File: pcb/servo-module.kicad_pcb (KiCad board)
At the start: 4 copper layers, 50 x 30 mm, 77 parts, among them J10 Power Out, J2 QWICC, J5 QWICC, J7 Power In, J9 AVR-UPDI-6, U1 ATtiny1616-MNR

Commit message: Updated worksheet template and logo
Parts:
- removed LOGO2: ~, CRGM Logos:FNWW Face 8mm
- added LOGO4: ~, CRGM Logos:CRGM Logo 5mm, B.Cu at (56.1, 153.1)
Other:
- board text removed: "FNWW"

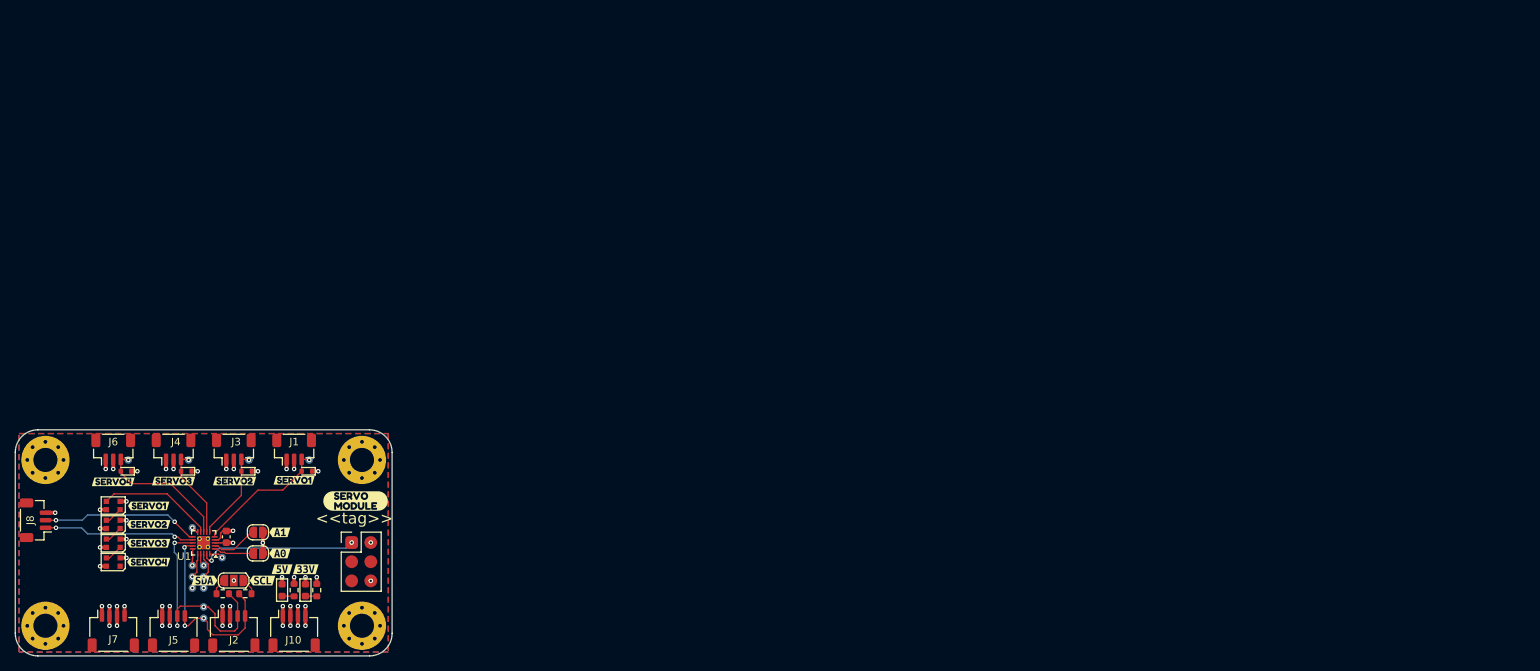
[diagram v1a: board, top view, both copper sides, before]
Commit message: Standardized parts; fixed title box
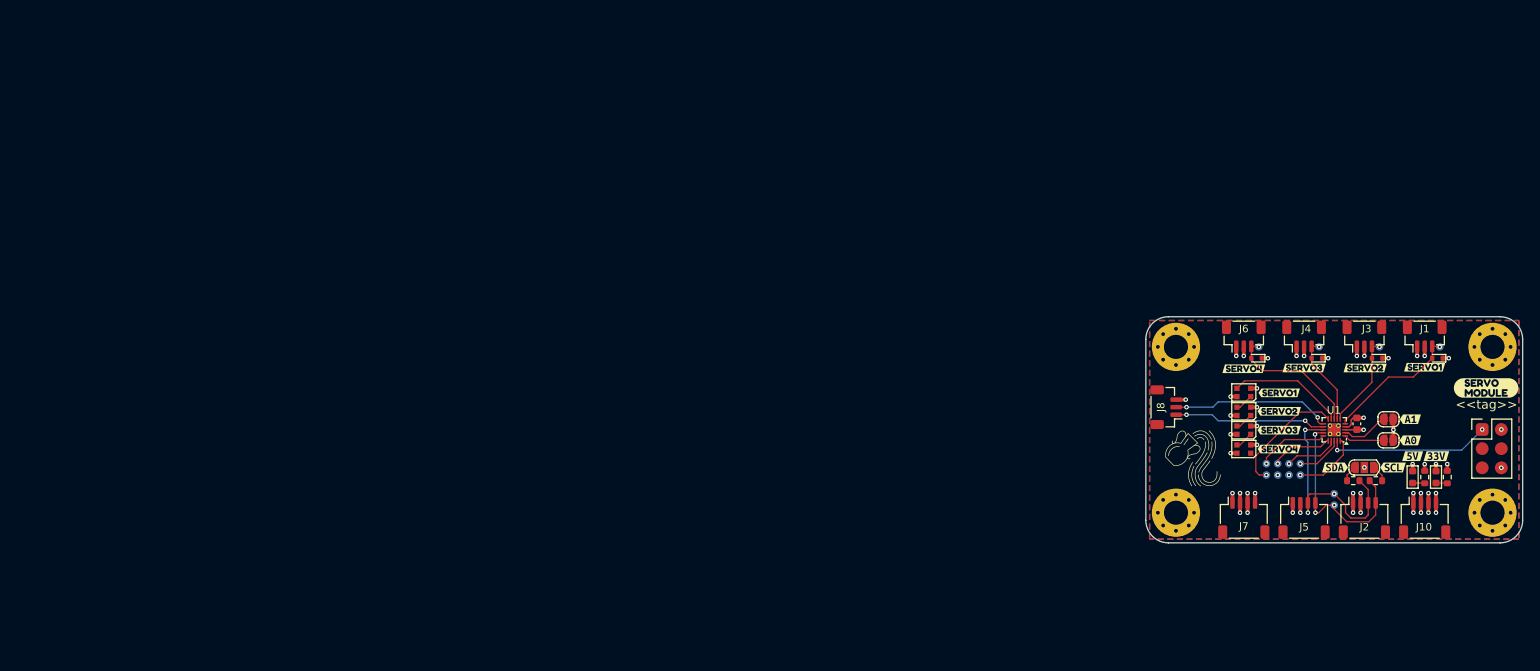
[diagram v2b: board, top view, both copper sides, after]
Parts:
- removed kibuzzard-685861B4: G***, kibuzzard-685861B4
- removed kibuzzard-685861D3: G***, kibuzzard-685861D3
- removed kibuzzard-685861D9: G***, kibuzzard-685861D9
- removed kibuzzard-68586205: G***, kibuzzard-68586205
- removed kibuzzard-6858621A: G***, kibuzzard-6858621A
- removed kibuzzard-68586228: G***, kibuzzard-68586228
- removed kibuzzard-68586245: G***, kibuzzard-68586245
- removed kibuzzard-68586260: G***, kibuzzard-68586260
- removed kibuzzard-68586282: G***, kibuzzard-68586282
- added LOGO2: ~, CRGM Logos:Aquarius Logo 8mm, F.Cu at (206.3, 138.8)
- added kibuzzard-6861B7EA: G***, kibuzzard-6861B7EA, B.Cu at (219.1, 137.1)
- added kibuzzard-6861B80B: G***, kibuzzard-6861B80B, B.Cu at (220.5, 137.1)
- added kibuzzard-6861B833: G***, kibuzzard-6861B833, B.Cu at (217.6, 137.1)
- added kibuzzard-6861B880: G***, kibuzzard-6861B880, B.Cu at (217.5, 143.6)
- added kibuzzard-6861B899: G***, kibuzzard-6861B899, B.Cu at (216.0, 143.6)
- added kibuzzard-6862CEAB: G***, kibuzzard-6862CEAB, B.Cu at (220.5, 143.6)
- added kibuzzard-6862CEB9: G***, kibuzzard-6862CEB9, B.Cu at (225.1, 142.0)
- added kibuzzard-6862CEC0: G***, kibuzzard-6862CEC0, B.Cu at (225.1, 146.5)
- added kibuzzard-6862CEE4: G***, kibuzzard-6862CEE4, B.Cu at (219.0, 143.6)
- C1: value .1uF -> 0.1uF
- R3: value 4.7k -> 4.7K
- R4: value 1k -> 1K
- moved LOGO4 162.6 mm to (216.9, 129.6)
- moved C1 150.7 mm to (228.0, 134.2)
- moved D1 150.7 mm to (238.7, 125.5)
- moved D10 150.7 mm to (214.7, 125.5)
- moved D2 150.7 mm to (235.4, 141.3)
- moved D3 150.7 mm to (238.5, 141.3)
- moved D4 150.7 mm to (213.0, 130.1)
- moved D5 150.7 mm to (213.0, 132.6)
- moved D6 150.7 mm to (213.0, 135.1)
- moved D7 150.7 mm to (213.0, 137.6)
- moved D8 150.7 mm to (230.7, 125.5)
- moved D9 150.7 mm to (222.7, 125.5)
- moved H1 150.7 mm to (204.0, 146.0)
- moved H2 150.7 mm to (246.0, 146.0)
- moved H3 150.7 mm to (246.0, 124.0)
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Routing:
- net /MCU/PB4: track 1.18 -> 16.3 mm
- net /MCU/PC0: track 2.22 -> 9.55 mm
- net /MCU/PA1: track 1.86 -> 8.98 mm
- net /MCU/PC2: track 1.72 -> 7.18 mm
- net /MCU/PC1: track 3.34 -> 8.23 mm
- net /MCU/PC3: track 3.55 -> 6.20 mm
- net +3.3V: track 16.6 -> 15.3 mm, vias 16 -> 15
- net GND: track 35.7 -> 34.4 mm, vias 31 -> 30

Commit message: Added panel options; moved PCB
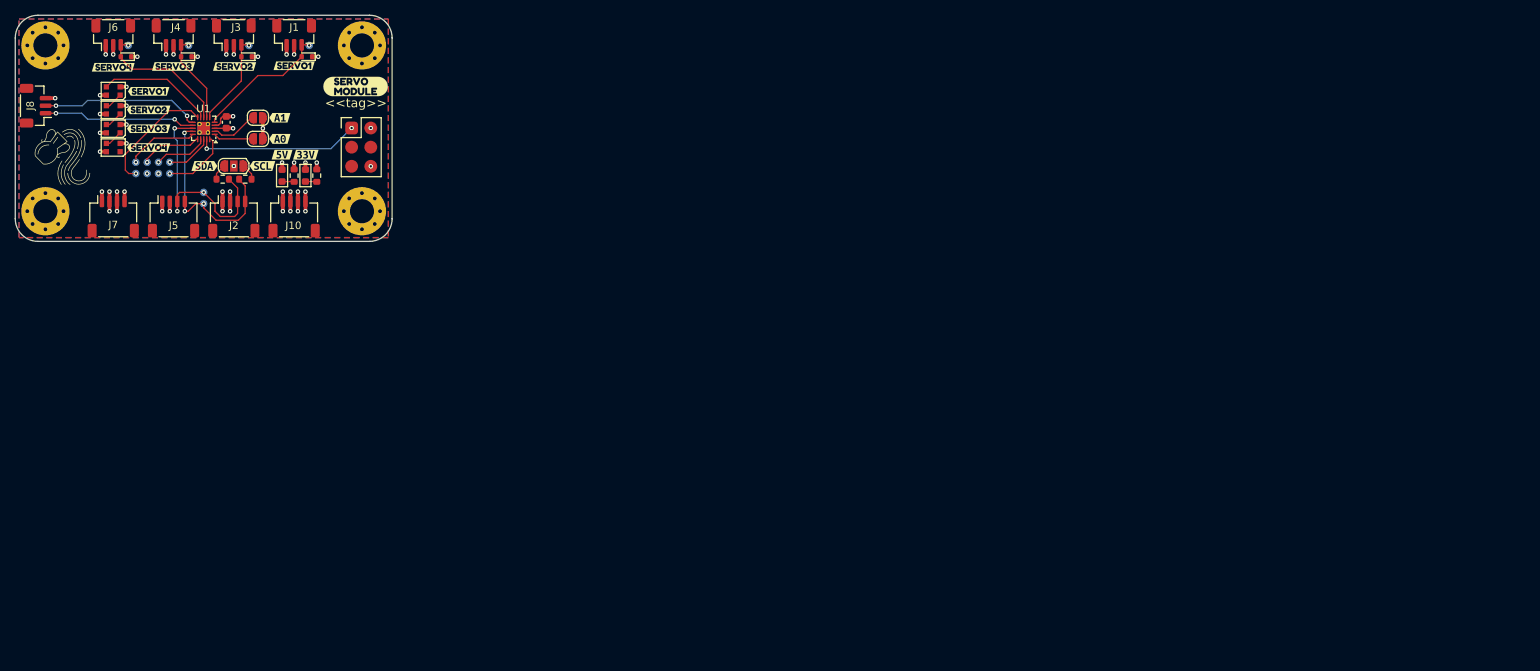
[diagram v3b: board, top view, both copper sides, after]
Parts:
- moved C1 155.2 mm to (78.0, 94.2)
- moved D1 155.2 mm to (88.7, 85.5)
- moved D10 155.2 mm to (64.7, 85.5)
- moved D2 155.2 mm to (85.4, 101.3)
- moved D3 155.2 mm to (88.5, 101.3)
- moved D4 155.2 mm to (63.0, 90.0)
- moved D5 155.2 mm to (63.0, 92.5)
- moved D6 155.2 mm to (63.0, 95.0)
- moved D7 155.2 mm to (63.0, 97.5)
- moved D8 155.2 mm to (80.7, 85.5)
- moved D9 155.2 mm to (72.7, 85.5)
- moved H1 155.2 mm to (54.0, 106.0)
- moved H2 155.2 mm to (96.0, 106.0)
- moved H3 155.2 mm to (96.0, 84.0)
- moved H4 155.2 mm to (54.0, 84.0)
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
